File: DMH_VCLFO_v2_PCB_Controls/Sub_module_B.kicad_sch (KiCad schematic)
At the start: 93 parts, among them J40 Conn_02x03_Odd_Even, J41 Conn_02x03_Odd_Even, J42 Conn_02x03_Odd_Even, J43 Conn_02x03_Odd_Even, J44 Conn_02x03_Odd_Even, J45 Conn_02x03_Odd_Even, Q18 BC548, Q19 BC548, Q20 MMBFJ113, Q21 MMBFJ113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

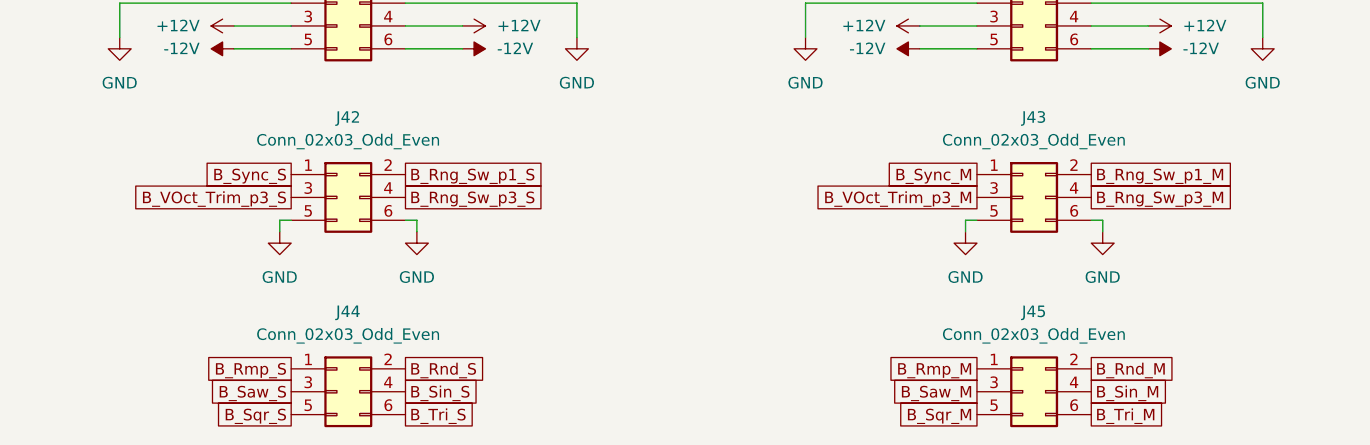
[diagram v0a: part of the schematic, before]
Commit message: Synced Controls PCB with Main
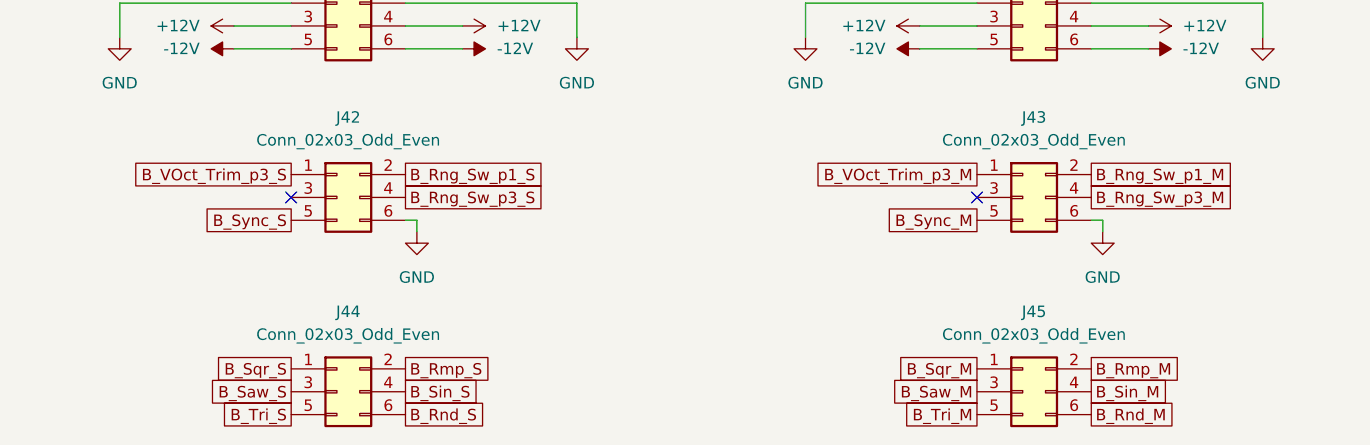
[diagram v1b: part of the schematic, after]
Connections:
- net B_Rmp_M: now also J45.2 (Pin_2); no longer J45.1 (Pin_1)
- net B_Rmp_S: now also J44.2 (Pin_2); no longer J44.1 (Pin_1)
- net B_Rnd_M: now also J45.6 (Pin_6); no longer J45.2 (Pin_2)
- net B_Rnd_S: now also J44.6 (Pin_6); no longer J44.2 (Pin_2)
- net B_Sqr_M: now also J45.1 (Pin_1); no longer J45.5 (Pin_5)
- net B_Sqr_S: now also J44.1 (Pin_1); no longer J44.5 (Pin_5)
- net B_Sync_M: now also J43.5 (Pin_5); no longer J43.1 (Pin_1)
- net B_Sync_S: now also J42.5 (Pin_5); no longer J42.1 (Pin_1)
- net B_Tri_M: now also J45.5 (Pin_5); no longer J45.6 (Pin_6)
- net B_Tri_S: now also J44.5 (Pin_5); no longer J44.6 (Pin_6)
- net B_VOct_Trim_p3_M: now also J43.1 (Pin_1); no longer J43.3 (Pin_3)
- net B_VOct_Trim_p3_S: now also J42.1 (Pin_1); no longer J42.3 (Pin_3)
- net GND: no longer J42.5 (Pin_5), J43.5 (Pin_5)
- no-connect marks 1 -> 3

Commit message: Generated Gerbers
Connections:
- net B_Rnd_S: now also U22.8, U22.9 (-); no longer U22.6 (-), U22.7
- net Comp_Ref: now also U22.2 (-); no longer U22.13 (-)
- net at D16.1 (K): now also U22.1; no longer U22.14
- net at Q20.1 (D), R116.1, R120.1: now also U22.14; no longer U22.1
- net at R116.2, R119.1: now also U22.13 (-); no longer U22.2 (-)
- net at R106.1, R99.2: now also U22.7; no longer U22.8
- net at C21.2, R118.1: now also U22.12 (+); no longer U22.3 (+)
- net at Q18.1 (C), R101.2, R99.1: now also U22.6 (-); no longer U22.9 (-)
- net at Q19.1 (C), R102.2, R111.1: now also U22.5 (+); no longer U22.10 (+)
- net at C24.1, R123.1: now also U22.3 (+); no longer U22.12 (+)
- net at C22.1, Q20.2 (S): now also U22.10 (+); no longer U22.5 (+)
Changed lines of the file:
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@@
 			)
 		)
+		(property "Function" ""
+			(at 243.84 254 0)
+			(effects
+				(font
+					(size 1.27 1.27)
+				)
+			)
+		)
 		(pin "10"
 		)
@@
 		(lib_id "Amplifier_Operational:TL074")
 		(at 69.85 95.25 0)
-		(unit 1)
+		(unit 4)
 		(exclude_from_sim no)
 		(in_bom yes)
@@
 				(path "/58f4306d-5387-4983-bb08-41a2313fd315/4bb1cd0d-fb31-47f1-80ec-81ed3bdfa89b"
 					(reference "U22")
-					(unit 1)
+					(unit 4)
 				)
 			)
@@
 		(lib_id "Amplifier_Operational:TL074")
 		(at 69.85 129.54 0)
-		(unit 4)
+		(unit 1)
 		(exclude_from_sim no)
 		(in_bom yes)
@@
 				(path "/58f4306d-5387-4983-bb08-41a2313fd315/4bb1cd0d-fb31-47f1-80ec-81ed3bdfa89b"
 					(reference "U22")
-					(unit 4)
+					(unit 1)
 				)
 			)
@@
 		(at 360.68 40.64 0)
 		(mirror x)
-		(unit 3)
+		(unit 2)
 		(exclude_from_sim no)
 		(in_bom yes)
@@
 				(path "/58f4306d-5387-4983-bb08-41a2313fd315/4bb1cd0d-fb31-47f1-80ec-81ed3bdfa89b"
 					(reference "U22")
-					(unit 3)
+					(unit 2)
 				)
 			)
@@
 		(lib_id "Amplifier_Operational:TL074")
 		(at 114.3 116.84 0)
-		(unit 2)
+		(unit 3)
 		(exclude_from_sim no)
 		(in_bom yes)
@@
 				(path "/58f4306d-5387-4983-bb08-41a2313fd315/4bb1cd0d-fb31-47f1-80ec-81ed3bdfa89b"
 					(reference "U22")
-					(unit 2)
+					(unit 3)
 				)
 			)
